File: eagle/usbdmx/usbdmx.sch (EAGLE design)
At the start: 35 parts, among them IC1 MAX3468CSA, IC2 MAX3468CSA, Q1 16MHz

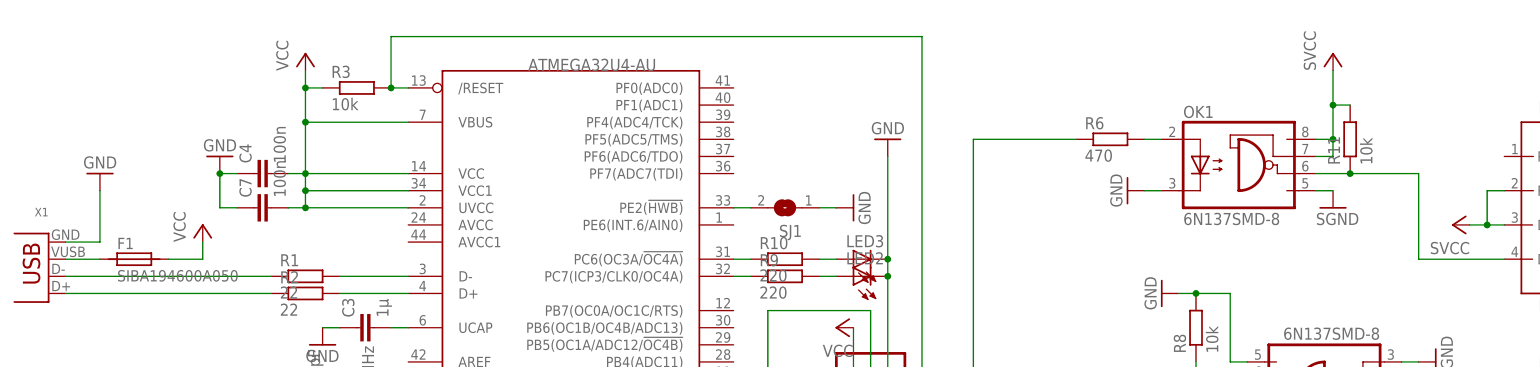
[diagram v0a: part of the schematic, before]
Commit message: fix usb port drill holes
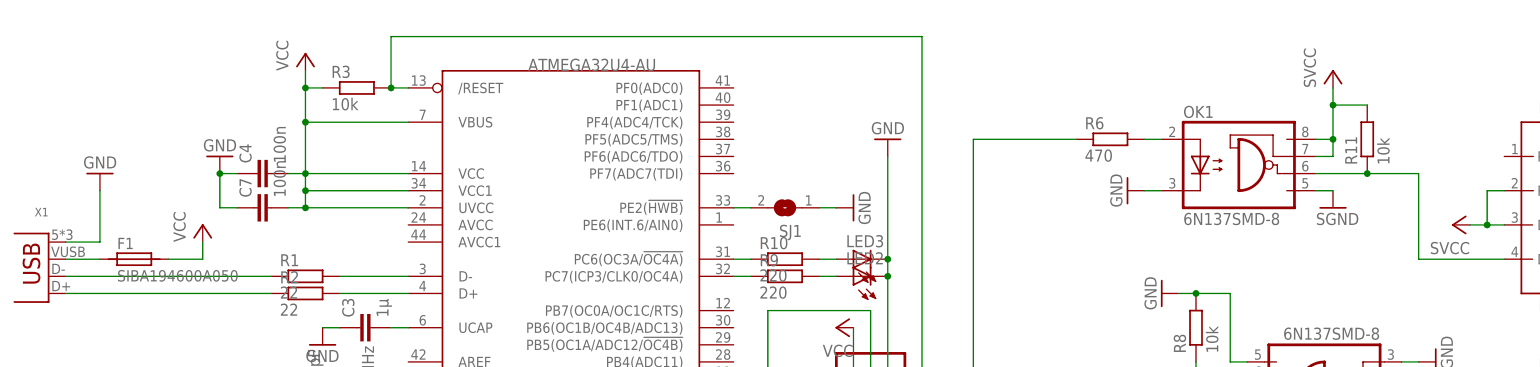
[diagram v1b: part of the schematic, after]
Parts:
- X1: device con-usb-3:USB-B-S -> con-usb-3:USB-B-S-R
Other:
- moved on the sheet: R11
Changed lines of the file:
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@@
 <part name="C2" library="rcl" deviceset="C-EU" device="C0805" value="22pF"/>
 <part name="GND1" library="supply1" deviceset="GND" device=""/>
-<part name="X1" library="con-usb-3" deviceset="USB" device="-B-S"/>
+<part name="X1" library="con-usb-3" deviceset="USB" device="-B-S-R"/>
 <part name="R1" library="rcl" deviceset="R-EU_" device="R0805" value="22"/>
 <part name="R2" library="rcl" deviceset="R-EU_" device="R0805" value="22"/>
@@
 <instance part="OK1" gate="A" x="175.26" y="78.74"/>
 <instance part="OK2" gate="A" x="185.42" y="48.26" rot="R180"/>
-<instance part="P+10" gate="VCC" x="187.96" y="96.52"/>
+<instance part="P+10" gate="VCC" x="187.96" y="93.98"/>
 <instance part="SGND7" gate="1" x="187.96" y="73.66"/>
 <instance part="P+11" gate="VCC" x="170.18" y="43.18" rot="R90"/>
@@
 <instance part="SJ1" gate="1" x="106.68" y="73.66" rot="R180"/>
 <instance part="DMXOUT" gate="G$1" x="287.02" y="76.2"/>
-<instance part="R11" gate="G$1" x="190.5" y="83.82" rot="R90"/>
+<instance part="R11" gate="G$1" x="193.04" y="83.82" rot="R90"/>
 </instances>
 <busses>
@@
 <pinref part="OK1" gate="A" pin="VCC"/>
 <wire x1="187.96" y1="83.82" x2="187.96" y2="88.9" width="0.1524" layer="91"/>
-<wire x1="187.96" y1="88.9" x2="187.96" y2="93.98" width="0.1524" layer="91"/>
+<wire x1="187.96" y1="88.9" x2="187.96" y2="91.44" width="0.1524" layer="91"/>
 <wire x1="185.42" y1="83.82" x2="187.96" y2="83.82" width="0.1524" layer="91"/>
 <junction x="187.96" y="83.82"/>
 <pinref part="R11" gate="G$1" pin="2"/>
-<wire x1="190.5" y1="88.9" x2="187.96" y2="88.9" width="0.1524" layer="91"/>
+<wire x1="193.04" y1="88.9" x2="187.96" y2="88.9" width="0.1524" layer="91"/>
 <junction x="187.96" y="88.9"/>
 </segment>
@@
 <wire x1="213.36" y1="66.04" x2="200.66" y2="66.04" width="0.1524" layer="91"/>
 <pinref part="OK1" gate="A" pin="VO"/>
-<wire x1="185.42" y1="78.74" x2="190.5" y2="78.74" width="0.1524" layer="91"/>
-<wire x1="190.5" y1="78.74" x2="200.66" y2="78.74" width="0.1524" layer="91"/>
+<wire x1="185.42" y1="78.74" x2="193.04" y2="78.74" width="0.1524" layer="91"/>
+<wire x1="193.04" y1="78.74" x2="200.66" y2="78.74" width="0.1524" layer="91"/>
 <wire x1="200.66" y1="78.74" x2="200.66" y2="66.04" width="0.1524" layer="91"/>
 <pinref part="R11" gate="G$1" pin="1"/>
-<junction x="190.5" y="78.74"/>
-</segment>
-</net>
+<junction x="193.04" y="78.74"/>
+</segment>
+</net>

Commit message: fix the polarity mixup on the secondary side
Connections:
- net SGND: now also C8.1, U$2.VOUT-; no longer C8.2, U$2.VOUT+
- net SVCC: now also C8.2, U$2.VOUT+; no longer C8.1, U$2.VOUT-
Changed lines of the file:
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@@
 <instance part="P+8" gate="VCC" x="109.22" y="5.08" rot="R90"/>
 <instance part="GND13" gate="1" x="109.22" y="10.16" rot="R270"/>
-<instance part="SGND" gate="1" x="180.34" y="2.54" rot="R90"/>
-<instance part="P+9" gate="VCC" x="180.34" y="10.16" rot="R270"/>
+<instance part="SGND" gate="1" x="180.34" y="10.16" rot="R90"/>
+<instance part="P+9" gate="VCC" x="180.34" y="2.54" rot="R270"/>
 <instance part="P+2" gate="VCC" x="251.46" y="45.72" rot="R270"/>
 <instance part="SGND1" gate="1" x="251.46" y="25.4" rot="R90"/>
@@
 <net name="SVCC" class="0">
 <segment>
-<pinref part="U$2" gate="G$1" pin="VOUT-"/>
-<wire x1="142.24" y1="10.16" x2="144.78" y2="10.16" width="0.1524" layer="91"/>
-<pinref part="P+9" gate="VCC" pin="VCC"/>
-<pinref part="C8" gate="G$1" pin="1"/>
-<wire x1="144.78" y1="10.16" x2="175.26" y2="10.16" width="0.1524" layer="91"/>
-<junction x="144.78" y="10.16"/>
-<pinref part="LED1" gate="G$1" pin="A"/>
-<wire x1="175.26" y1="10.16" x2="177.8" y2="10.16" width="0.1524" layer="91"/>
-<wire x1="172.72" y1="5.08" x2="175.26" y2="5.08" width="0.1524" layer="91"/>
-<wire x1="175.26" y1="5.08" x2="175.26" y2="10.16" width="0.1524" layer="91"/>
-<junction x="175.26" y="10.16"/>
-</segment>
-<segment>
 <pinref part="IC1" gate="G$1" pin="VCC"/>
 <wire x1="246.38" y1="45.72" x2="248.92" y2="45.72" width="0.1524" layer="91"/>
@@
 <junction x="187.96" y="88.9"/>
 </segment>
+<segment>
+<pinref part="LED1" gate="G$1" pin="A"/>
+<wire x1="172.72" y1="5.08" x2="175.26" y2="5.08" width="0.1524" layer="91"/>
+<wire x1="175.26" y1="5.08" x2="175.26" y2="2.54" width="0.1524" layer="91"/>
+<pinref part="P+9" gate="VCC" pin="VCC"/>
+<wire x1="175.26" y1="2.54" x2="177.8" y2="2.54" width="0.1524" layer="91"/>
+<pinref part="U$2" gate="G$1" pin="VOUT+"/>
+<wire x1="142.24" y1="5.08" x2="142.24" y2="2.54" width="0.1524" layer="91"/>
+<pinref part="C8" gate="G$1" pin="2"/>
+<wire x1="142.24" y1="2.54" x2="144.78" y2="2.54" width="0.1524" layer="91"/>
+<junction x="144.78" y="2.54"/>
+<wire x1="175.26" y1="2.54" x2="144.78" y2="2.54" width="0.1524" layer="91"/>
+<junction x="175.26" y="2.54"/>
+</segment>
 </net>
 <net name="SGND" class="0">
@@
 </segment>
 <segment>
-<pinref part="U$2" gate="G$1" pin="VOUT+"/>
-<wire x1="142.24" y1="5.08" x2="142.24" y2="2.54" width="0.1524" layer="91"/>
-<pinref part="C8" gate="G$1" pin="2"/>
-<wire x1="142.24" y1="2.54" x2="144.78" y2="2.54" width="0.1524" layer="91"/>
-<wire x1="144.78" y1="2.54" x2="149.86" y2="2.54" width="0.1524" layer="91"/>
-<junction x="144.78" y="2.54"/>
-<wire x1="149.86" y1="2.54" x2="149.86" y2="5.08" width="0.1524" layer="91"/>
-<pinref part="R4" gate="G$1" pin="1"/>
-<wire x1="149.86" y1="5.08" x2="152.4" y2="5.08" width="0.1524" layer="91"/>
-<pinref part="SGND" gate="1" pin="GND"/>
-<wire x1="149.86" y1="2.54" x2="177.8" y2="2.54" width="0.1524" layer="91"/>
-<junction x="149.86" y="2.54"/>
-</segment>
-<segment>
 <pinref part="SGND5" gate="1" pin="GND"/>
 <wire x1="271.78" y1="83.82" x2="271.78" y2="78.74" width="0.1524" layer="91"/>
@@
 <wire x1="271.78" y1="78.74" x2="276.86" y2="78.74" width="0.1524" layer="91"/>
 </segment>
-</net>
+<segment>
+<pinref part="U$2" gate="G$1" pin="VOUT-"/>
+<wire x1="142.24" y1="10.16" x2="144.78" y2="10.16" width="0.1524" layer="91"/>
+<pinref part="C8" gate="G$1" pin="1"/>
+<wire x1="144.78" y1="10.16" x2="149.86" y2="10.16" width="0.1524" layer="91"/>
+<junction x="144.78" y="10.16"/>
+<pinref part="R4" gate="G$1" pin="1"/>
+<wire x1="149.86" y1="10.16" x2="177.8" y2="10.16" width="0.1524" layer="91"/>
+<wire x1="149.86" y1="5.08" x2="152.4" y2="5.08" width="0.1524" layer="91"/>
+<wire x1="149.86" y1="10.16" x2="149.86" y2="5.08" width="0.1524" layer="91"/>
+<junction x="149.86" y="10.16"/>
+<pinref part="SGND" gate="1" pin="GND"/>
+</segment>
+</net>
